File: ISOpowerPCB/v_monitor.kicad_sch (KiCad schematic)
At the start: 20 parts, among them U15 TL431DBZ, U16 TL431DBZ, U17 TL431DBZ, U18 TL431DBZ

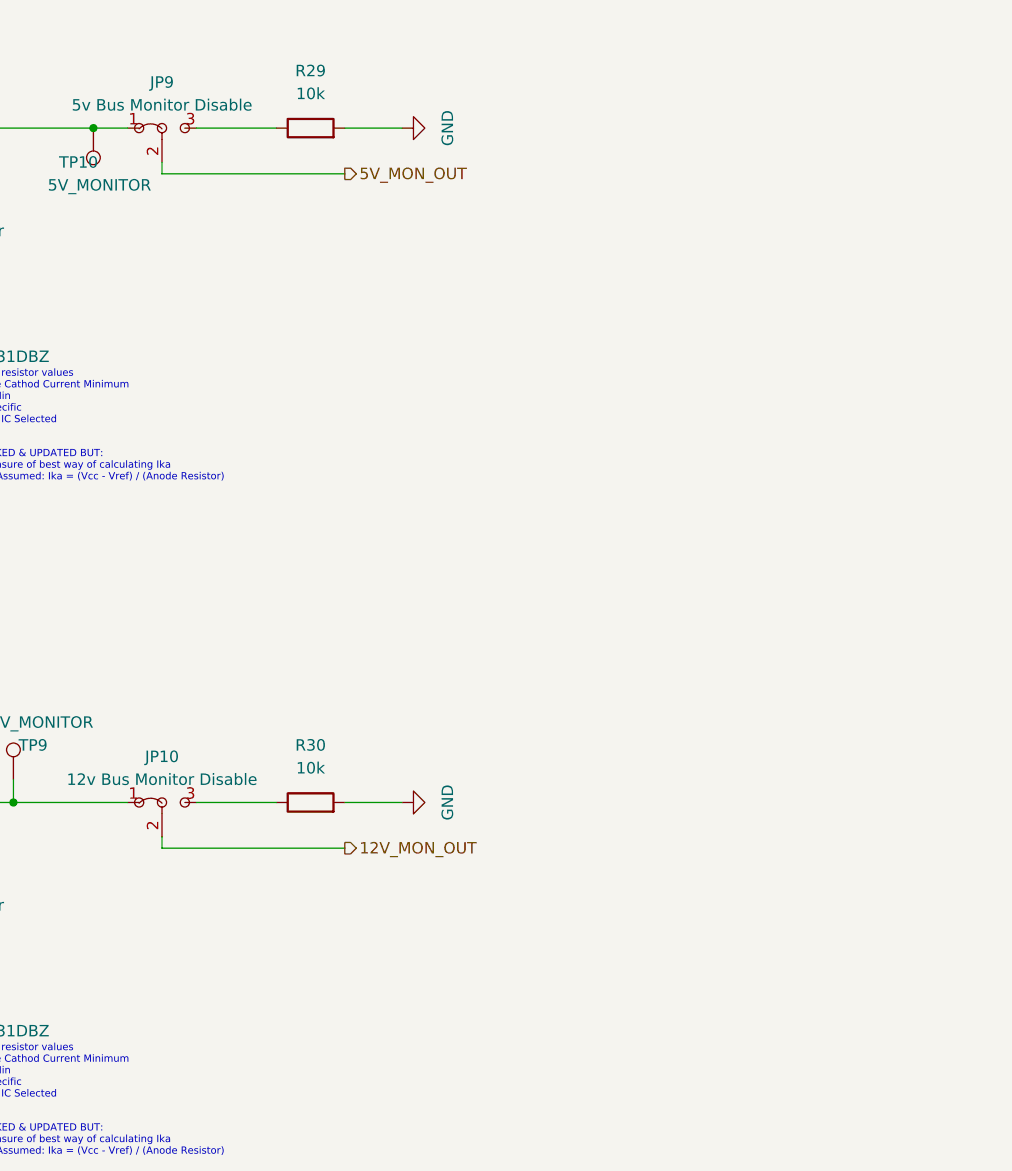
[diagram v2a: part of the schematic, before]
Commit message: adding logic for fault indication
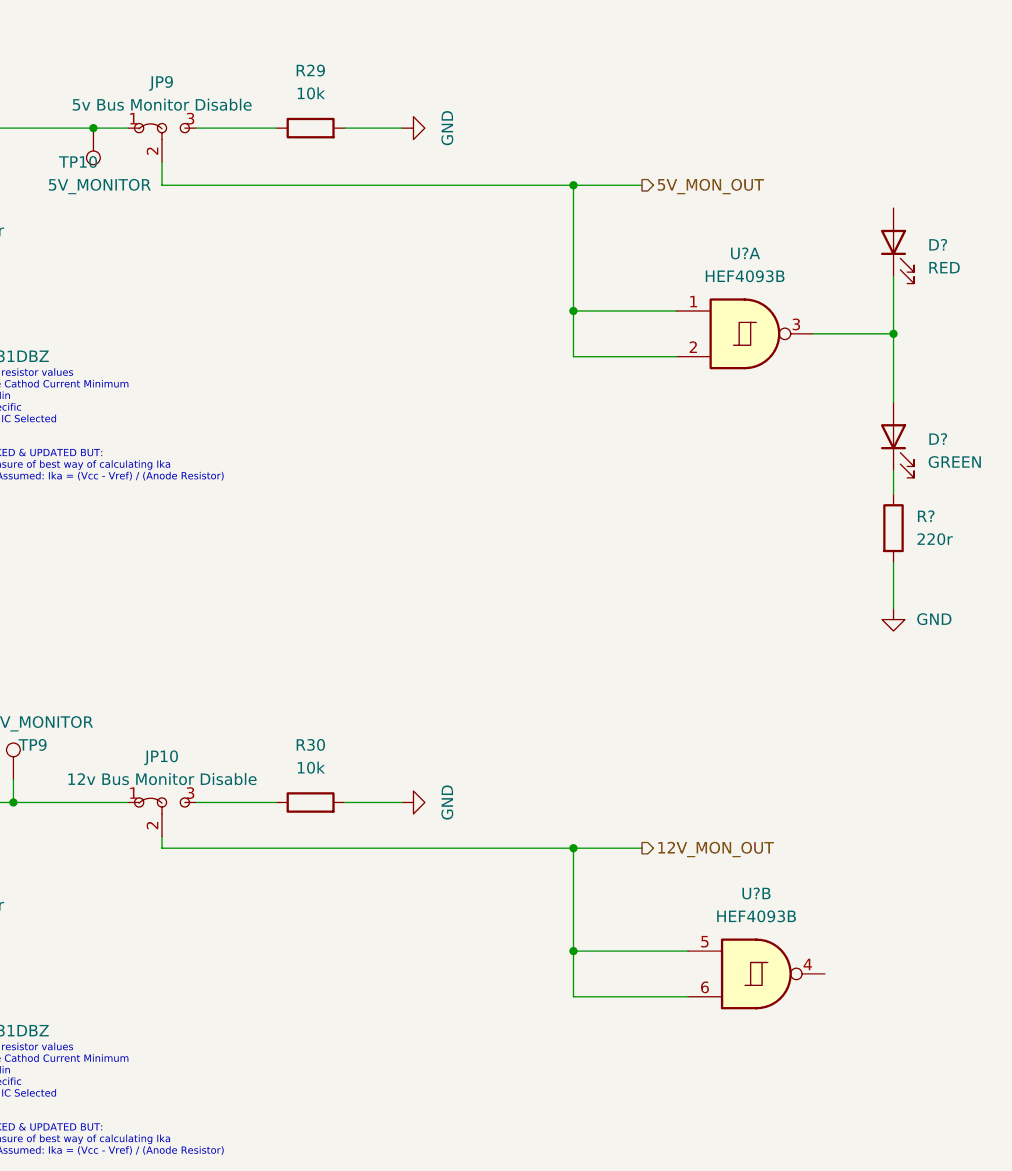
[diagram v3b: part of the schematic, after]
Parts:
- added D?: GREEN, symbol Device:LED
- added D?: RED, symbol Device:LED
- added R?: 220r, Resistor_SMD:R_0805_2012Metric_Pad1.20x1.40mm_HandSolder, symbol 000_Resistors_Immo:Resistor_0805
- added U? (x2): HEF4093B, symbol 4xxx:HEF4093B
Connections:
- net 12V_MON_OUT: now also U?.5, U?.6
- net 5V_MON_OUT: now also U?.1, U?.2
- net GND: now also R?.2
- new net: D?.1 (K), R?.1
- new net: D?.1 (K), D?.2 (A), U?.3
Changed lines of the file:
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@@
 (kicad_sch (version 20211123) (generator eeschema)
   (paper "A4")
+  (junction (at 179.07 128.27) (diameter 0) (color 0 0 0 0)
+  )
   (junction (at 99.06 153.67) (diameter 0) (color 0 0 0 0)
   )
+  (junction (at 214.63 59.69) (diameter 0) (color 0 0 0 0)
+  )
   (junction (at 99.06 135.89) (diameter 0) (color 0 0 0 0)
   )
@@
   (junction (at 73.66 66.04) (diameter 0) (color 0 0 0 0)
   )
+  (junction (at 179.07 43.18) (diameter 0) (color 0 0 0 0)
+  )
+  (junction (at 179.07 116.84) (diameter 0) (color 0 0 0 0)
+  )
   (junction (at 73.66 48.26) (diameter 0) (color 0 0 0 0)
   )
@@
   (junction (at 73.66 140.97) (diameter 0) (color 0 0 0 0)
   )
+  (junction (at 179.07 57.15) (diameter 0) (color 0 0 0 0)
+  )
   (wire (pts (xy 99.06 151.13) (xy 99.06 153.67))
     (stroke (width 0) (type default) (color 0 0 0 0))
@@
     (stroke (width 0) (type default) (color 0 0 0 0))
   )
+  (wire (pts (xy 179.07 43.18) (xy 133.35 43.18))
+    (stroke (width 0) (type default) (color 0 0 0 0))
+  )
   (wire (pts (xy 85.09 143.51) (xy 85.09 153.67))
     (stroke (width 0) (type default) (color 0 0 0 0))
@@
     (stroke (width 0) (type default) (color 0 0 0 0))
   )
+  (wire (pts (xy 214.63 59.69) (xy 214.63 53.34))
+    (stroke (width 0) (type default) (color 0 0 0 0))
+  )
   (wire (pts (xy 153.67 111.76) (xy 160.02 111.76))
     (stroke (width 0) (type default) (color 0 0 0 0))
@@
     (stroke (width 0) (type default) (color 0 0 0 0))
   )
+  (wire (pts (xy 205.74 59.69) (xy 214.63 59.69))
+    (stroke (width 0) (type default) (color 0 0 0 0))
+  )
   (wire (pts (xy 99.06 125.73) (xy 99.06 123.19))
     (stroke (width 0) (type default) (color 0 0 0 0))
@@
     (stroke (width 0) (type default) (color 0 0 0 0))
   )
+  (wire (pts (xy 214.63 59.69) (xy 214.63 67.31))
+    (stroke (width 0) (type default) (color 0 0 0 0))
+  )
+  (wire (pts (xy 190.5 57.15) (xy 179.07 57.15))
+    (stroke (width 0) (type default) (color 0 0 0 0))
+  )
   (wire (pts (xy 73.66 63.5) (xy 73.66 66.04))
     (stroke (width 0) (type default) (color 0 0 0 0))
@@
     (stroke (width 0) (type default) (color 0 0 0 0))
   )
-  (wire (pts (xy 133.35 40.64) (xy 133.35 41.91))
+  (wire (pts (xy 133.35 40.64) (xy 133.35 43.18))
     (stroke (width 0) (type default) (color 0 0 0 0))
   )
@@
     (stroke (width 0) (type default) (color 0 0 0 0))
   )
+  (wire (pts (xy 191.77 128.27) (xy 179.07 128.27))
+    (stroke (width 0) (type default) (color 0 0 0 0))
+  )
   (wire (pts (xy 133.35 115.57) (xy 133.35 116.84))
     (stroke (width 0) (type default) (color 0 0 0 0))
@@
     (stroke (width 0) (type default) (color 0 0 0 0))
   )
+  (wire (pts (xy 179.07 133.35) (xy 179.07 128.27))
+    (stroke (width 0) (type default) (color 0 0 0 0))
+  )
   (wire (pts (xy 73.66 153.67) (xy 85.09 153.67))
     (stroke (width 0) (type default) (color 0 0 0 0))
   )
+  (wire (pts (xy 179.07 57.15) (xy 179.07 43.18))
+    (stroke (width 0) (type default) (color 0 0 0 0))
+  )
   (wire (pts (xy 99.06 60.96) (xy 85.09 60.96))
     (stroke (width 0) (type default) (color 0 0 0 0))
@@
     (stroke (width 0) (type default) (color 0 0 0 0))
   )
-  (wire (pts (xy 153.67 116.84) (xy 133.35 116.84))
+  (wire (pts (xy 186.69 116.84) (xy 179.07 116.84))
     (stroke (width 0) (type default) (color 0 0 0 0))
   )
@@
     (stroke (width 0) (type default) (color 0 0 0 0))
   )
+  (wire (pts (xy 214.63 85.09) (xy 214.63 90.17))
+    (stroke (width 0) (type default) (color 0 0 0 0))
+  )
   (wire (pts (xy 25.4 21.59) (xy 30.48 21.59))
     (stroke (width 0) (type default) (color 0 0 0 0))
   )
+  (wire (pts (xy 214.63 74.93) (xy 214.63 77.47))
+    (stroke (width 0) (type default) (color 0 0 0 0))
+  )
+  (wire (pts (xy 179.07 128.27) (xy 179.07 116.84))
+    (stroke (width 0) (type default) (color 0 0 0 0))
+  )
   (wire (pts (xy 109.22 138.43) (xy 109.22 153.67))
     (stroke (width 0) (type default) (color 0 0 0 0))
@@
     (stroke (width 0) (type default) (color 0 0 0 0))
   )
+  (wire (pts (xy 190.5 62.23) (xy 179.07 62.23))
+    (stroke (width 0) (type default) (color 0 0 0 0))
+  )
   (wire (pts (xy 99.06 133.35) (xy 99.06 135.89))
     (stroke (width 0) (type default) (color 0 0 0 0))
   )
+  (wire (pts (xy 191.77 133.35) (xy 179.07 133.35))
+    (stroke (width 0) (type default) (color 0 0 0 0))
+  )
   (wire (pts (xy 109.22 111.76) (xy 116.84 111.76))
     (stroke (width 0) (type default) (color 0 0 0 0))
   )
-  (wire (pts (xy 153.67 41.91) (xy 133.35 41.91))
+  (wire (pts (xy 179.07 116.84) (xy 133.35 116.84))
+    (stroke (width 0) (type default) (color 0 0 0 0))
+  )
+  (wire (pts (xy 179.07 62.23) (xy 179.07 57.15))
+    (stroke (width 0) (type default) (color 0 0 0 0))
+  )
+  (wire (pts (xy 186.69 43.18) (xy 179.07 43.18))
     (stroke (width 0) (type default) (color 0 0 0 0))
   )
@@
     (effects (font (size 1.27 1.27)) (justify left))
   )
-  (hierarchical_label "12V_MON_OUT" (shape output) (at 153.67 116.84 0)
+  (hierarchical_label "12V_MON_OUT" (shape output) (at 186.69 116.84 0)
     (effects (font (size 1.27 1.27)) (justify left))
   )
@@
     (effects (font (size 1.27 1.27)) (justify left))
   )
-  (hierarchical_label "5V_MON_OUT" (shape output) (at 153.67 41.91 0)
+  (hierarchical_label "5V_MON_OUT" (shape output) (at 186.69 43.18 0)
     (effects (font (size 1.27 1.27)) (justify left))
   )
@@
     (pin "3")
   )
+  (symbol (lib_id "Device:LED") (at 214.63 71.12 90) (unit 1)
+    (in_bom yes) (on_board yes) (fields_autoplaced)
+    (property "Reference" "D?" (id 0) (at 218.44 71.4374 90)
+      (effects (font (size 1.27 1.27)) (justify right))
+    )
+    (property "Value" "GREEN" (id 1) (at 218.44 73.9774 90)
+      (effects (font (size 1.27 1.27)) (justify right))
+    )
+    (property "Footprint" "" (id 2) (at 214.63 71.12 0)
+      (effects (font (size 1.27 1.27)) hide)
+    )
+    (property "Datasheet" "~" (id 3) (at 214.63 71.12 0)
+      (effects (font (size 1.27 1.27)) hide)
+    )
+    (pin "1")
+    (pin "2")
+  )
   (symbol (lib_id "000_Resistors_Immo:Resistor_0805") (at 149.86 111.76 90) (unit 1)
     (in_bom yes) (on_board yes) (fields_autoplaced)
@@
     (pin "2")
   )
+  (symbol (lib_id "Device:LED") (at 214.63 49.53 90) (unit 1)
+    (in_bom yes) (on_board yes) (fields_autoplaced)
+    (property "Reference" "D?" (id 0) (at 218.44 49.8474 90)
+      (effects (font (size 1.27 1.27)) (justify right))
+    )
+    (property "Value" "RED" (id 1) (at 218.44 52.3874 90)
+      (effects (font (size 1.27 1.27)) (justify right))
+    )
+    (property "Footprint" "" (id 2) (at 214.63 49.53 0)
+      (effects (font (size 1.27 1.27)) hide)
+    )
+    (property "Datasheet" "~" (id 3) (at 214.63 49.53 0)
+      (effects (font (size 1.27 1.27)) hide)
+    )
+    (pin "1")
+    (pin "2")
+  )
   (symbol (lib_id "000_Resistors_Immo:Resistor_0805") (at 99.06 72.39 0) (unit 1)
     (in_bom yes) (on_board yes) (fields_autoplaced)
@@
     )
     (property "Datasheet" "~" (id 3) (at 99.06 72.39 0)
+      (effects (font (size 1.27 1.27)) hide)
+    )
+    (pin "1")
+    (pin "2")
+  )
+  (symbol (lib_id "000_Resistors_Immo:Resistor_0805") (at 214.63 81.28 0) (unit 1)
+    (in_bom yes) (on_board yes) (fields_autoplaced)
+    (property "Reference" "R?" (id 0) (at 217.17 80.0099 0)
+      (effects (font (size 1.27 1.27)) (justify left))
+    )
+    (property "Value" "220r" (id 1) (at 217.17 82.5499 0)
+      (effects (font (size 1.27 1.27)) (justify left))
+    )
+    (property "Footprint" "Resistor_SMD:R_0805_2012Metric_Pad1.20x1.40mm_HandSolder" (id 2) (at 212.852 81.28 90)
+      (effects (font (size 1.27 1.27)) hide)
+    )
+    (property "Datasheet" "~" (id 3) (at 214.63 81.28 0)
       (effects (font (size 1.27 1.27)) hide)
     )
@@
     (property "Datasheet" "http://www.ti.com/lit/ds/symlink/tl431.pdf" (id 3) (at 85.09 140.97 0)
       (effects (font (size 1.27 1.27) italic) hide)
+    )
+    (pin "1")
+    (pin "2")
+    (pin "3")
+  )
+  (symbol (lib_id "4xxx:HEF4093B") (at 198.12 59.69 0) (unit 1)
+    (in_bom yes) (on_board yes) (fields_autoplaced)
+    (property "Reference" "U?" (id 0) (at 198.12 50.8 0))
+    (property "Value" "HEF4093B" (id 1) (at 198.12 53.34 0))
+    (property "Footprint" "" (id 2) (at 198.12 59.69 0)
+      (effects (font (size 1.27 1.27)) hide)
+    )
+    (property "Datasheet" "https://assets.nexperia.com/documents/data-sheet/HEF4093B.pdf" (id 3) (at 198.12 59.69 0)
+      (effects (font (size 1.27 1.27)) hide)
     )
     (pin "1")
@@
     (pin "1")
   )
+  (symbol (lib_id "4xxx:HEF4093B") (at 199.39 130.81 0) (unit 2)
+    (in_bom yes) (on_board yes) (fields_autoplaced)
+    (property "Reference" "U?" (id 0) (at 199.39 121.92 0))
+    (property "Value" "HEF4093B" (id 1) (at 199.39 124.46 0))
+    (property "Footprint" "" (id 2) (at 199.39 130.81 0)
+      (effects (font (size 1.27 1.27)) hide)
+    )
+    (property "Datasheet" "https://assets.nexperia.com/documents/data-sheet/HEF4093B.pdf" (id 3) (at 199.39 130.81 0)
+      (effects (font (size 1.27 1.27)) hide)
+    )
+    (pin "4")
+    (pin "5")
+    (pin "6")
+  )
   (symbol (lib_id "000_Resistors_Immo:Resistor_0805") (at 73.66 59.69 0) (unit 1)
     (in_bom yes) (on_board yes) (fields_autoplaced)
@@
     (pin "2")
   )
+  (symbol (lib_id "power:GND") (at 214.63 90.17 0) (unit 1)
+    (in_bom yes) (on_board yes) (fields_autoplaced)
+    (property "Reference" "#PWR?" (id 0) (at 214.63 96.52 0)
+      (effects (font (size 1.27 1.27)) hide)
+    )
+    (property "Value" "GND" (id 1) (at 217.17 91.4399 0)
+      (effects (font (size 1.27 1.27)) (justify left))
+    )
+    (property "Footprint" "" (id 2) (at 214.63 90.17 0)
+      (effects (font (size 1.27 1.27)) hide)
+    )
+    (property "Datasheet" "" (id 3) (at 214.63 90.17 0)
+      (effects (font (size 1.27 1.27)) hide)
+    )
+    (pin "1")
+  )
   (symbol (lib_id "000_Resistors_Immo:Resistor_0805") (at 73.66 72.39 0) (unit 1)

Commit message: uurgh libraries
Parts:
- added C30: 100n, Capacitor_SMD:C_0805_2012Metric_Pad1.18x1.45mm_HandSolder, symbol 000_Capacitor_film_immo:cap_film_0805
- added D6: GREEN, symbol Device:LED
- added D8: RED, symbol Device:LED
- added R31, R32, R34: 220r, Resistor_SMD:R_0805_2012Metric_Pad1.20x1.40mm_HandSolder, symbol 000_Resistors_Immo:Resistor_0805
- added unit 4 of U19
- added unit 5 of U19
- added unit 3 of U19
- gave numbers to parts that had none: 4
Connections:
- net GND: now also C30.2, R31.2, R32.2, R34.2, U19.7 (GND)
- net MCU_5V_IN: now also C30.1, U19.14 (VCC)
- net at D5.1 (K): now also R31.1; no longer R33.1
- net at D5.2 (A), U19.3: now also U19.8, U19.9; no longer D7.1 (K)
- net at D7.2 (A): now also U19.10
- net at U19.4: now also D6.2 (A), U19.12, U19.13
- new net: D8.1 (K), R34.1
- new net: D8.2 (A), U19.11
- new net: D7.1 (K), R33.1
- new net: D6.1 (K), R32.1
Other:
- moved on the sheet: D5, D7, R33

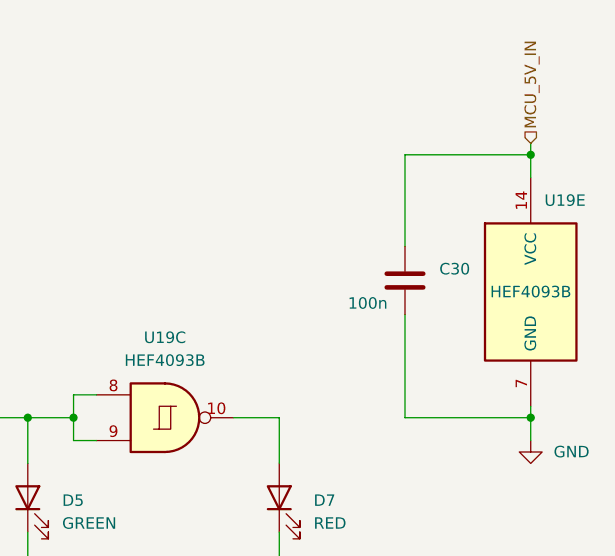
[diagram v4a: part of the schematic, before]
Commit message: fixed most electrical rules check violations
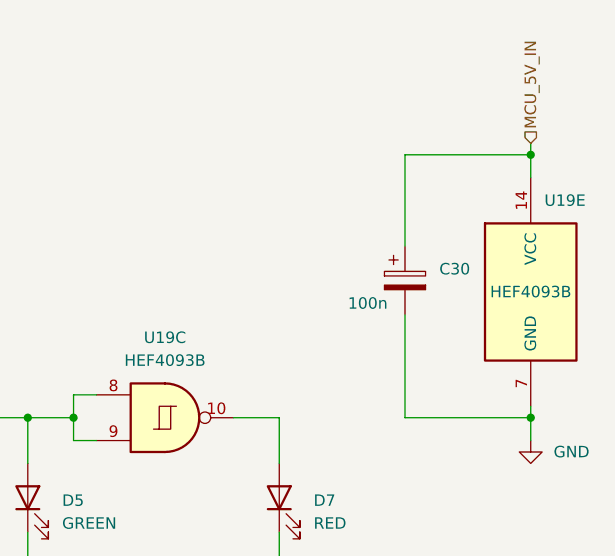
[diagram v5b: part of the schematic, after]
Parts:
- C30: footprint Capacitor_SMD:C_0805_2012Metric_Pad1.18x1.45mm_HandSolder -> Capacitor_SMD:CP_Elec_10x10; symbol 000_Capacitor_film_immo:cap_film_0805 -> 000_Capacitor_Electrolytic_Immo:100u
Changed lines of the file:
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@@
     (pin "3")
   )
-  (symbol (lib_id "000_Capacitor_film_immo:cap_film_0805") (at 251.46 44.45 0) (unit 1)
+  (symbol (lib_id "000_Capacitor_Electrolytic_Immo:100u") (at 251.46 44.45 0) (unit 1)
     (in_bom yes) (on_board yes)
     (property "Reference" "C30" (id 0) (at 255.27 43.1799 0)
@@
       (effects (font (size 1.27 1.27)) (justify left))
     )
-    (property "Footprint" "Capacitor_SMD:C_0805_2012Metric_Pad1.18x1.45mm_HandSolder" (id 2) (at 252.73 54.61 0)
+    (property "Footprint" "Capacitor_SMD:CP_Elec_10x10" (id 2) (at 252.4252 48.26 0)
       (effects (font (size 1.27 1.27)) hide)
     )

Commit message: Footprint Associations 50% complete
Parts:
- removed C30: 100n, Capacitor_SMD:CP_Elec_10x10, symbol 000_Capacitor_Electrolytic_Immo:100u
- added C30: 100n, Capacitor_SMD:C_0805_2012Metric_Pad1.18x1.45mm_HandSolder, symbol 000_Capacitor_Film_Immo:cap_film_0805
- D5, D6, D7, D8: footprint (none) -> LED_SMD:LED_0805_2012Metric_Pad1.15x1.40mm_HandSolder
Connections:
- net GND: now also C30.2
- net MCU_5V_IN: now also C30.1
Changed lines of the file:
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@@
       (effects (font (size 1.27 1.27)) (justify right))
     )
-    (property "Footprint" "" (id 2) (at 209.55 68.58 0)
+    (property "Footprint" "LED_SMD:LED_0805_2012Metric_Pad1.15x1.40mm_HandSolder" (id 2) (at 209.55 68.58 0)
       (effects (font (size 1.27 1.27)) hide)
     )
     (property "Datasheet" "~" (id 3) (at 209.55 68.58 0)
+      (effects (font (size 1.27 1.27)) hide)
+    )
+    (pin "1")
+    (pin "2")
+  )
+  (symbol (lib_id "000_Capacitor_Film_Immo:cap_film_0805") (at 251.46 44.45 0) (unit 1)
+    (in_bom yes) (on_board yes)
+    (property "Reference" "C30" (id 0) (at 243.84 43.18 0)
+      (effects (font (size 1.27 1.27)) (justify left))
+    )
+    (property "Value" "100n" (id 1) (at 242.57 46.99 0)
+      (effects (font (size 1.27 1.27)) (justify left))
+    )
+    (property "Footprint" "Capacitor_SMD:C_0805_2012Metric_Pad1.18x1.45mm_HandSolder" (id 2) (at 252.73 54.61 0)
+      (effects (font (size 1.27 1.27)) hide)
+    )
+    (property "Datasheet" "~" (id 3) (at 251.46 44.45 0)
       (effects (font (size 1.27 1.27)) hide)
     )
@@
       (effects (font (size 1.27 1.27)) (justify right))
     )
-    (property "Footprint" "" (id 2) (at 237.49 138.43 0)
+    (property "Footprint" "LED_SMD:LED_0805_2012Metric_Pad1.15x1.40mm_HandSolder" (id 2) (at 237.49 138.43 0)
       (effects (font (size 1.27 1.27)) hide)
     )
@@
       (effects (font (size 1.27 1.27)) (justify right))
     )
-    (property "Footprint" "" (id 2) (at 237.49 68.58 0)
+    (property "Footprint" "LED_SMD:LED_0805_2012Metric_Pad1.15x1.40mm_HandSolder" (id 2) (at 237.49 68.58 0)
       (effects (font (size 1.27 1.27)) hide)
     )
@@
       (effects (font (size 1.27 1.27)) (justify right))
     )
-    (property "Footprint" "" (id 2) (at 209.55 138.43 0)
+    (property "Footprint" "LED_SMD:LED_0805_2012Metric_Pad1.15x1.40mm_HandSolder" (id 2) (at 209.55 138.43 0)
       (effects (font (size 1.27 1.27)) hide)
     )
@@
     (pin "3")
   )
-  (symbol (lib_id "000_Capacitor_Electrolytic_Immo:100u") (at 251.46 44.45 0) (unit 1)
-    (in_bom yes) (on_board yes)
-    (property "Reference" "C30" (id 0) (at 255.27 43.1799 0)
-      (effects (font (size 1.27 1.27)) (justify left))
-    )
-    (property "Value" "100n" (id 1) (at 245.11 46.99 0)
-      (effects (font (size 1.27 1.27)) (justify left))
-    )
-    (property "Footprint" "Capacitor_SMD:CP_Elec_10x10" (id 2) (at 252.4252 48.26 0)
-      (effects (font (size 1.27 1.27)) hide)
-    )
-    (property "Datasheet" "~" (id 3) (at 251.46 44.45 0)
-      (effects (font (size 1.27 1.27)) hide)
-    )
-    (pin "1")
-    (pin "2")
-  )
   (symbol (lib_id "000_Resistors_Immo:Resistor_0805") (at 99.06 129.54 0) (unit 1)
